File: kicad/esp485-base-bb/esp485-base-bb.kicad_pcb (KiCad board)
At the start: 2 copper layers, 25.4 x 59.7 mm, 20 parts, among them J1 Conn_01x03, J10 Conn_01x04, J11 Conn_01x04, J12 Conn_01x08, J2 Conn_01x03, J3 Conn_01x08, J4 Conn_01x08, J5 Conn_01x04, J6 Conn_01x03, J7 Conn_01x03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

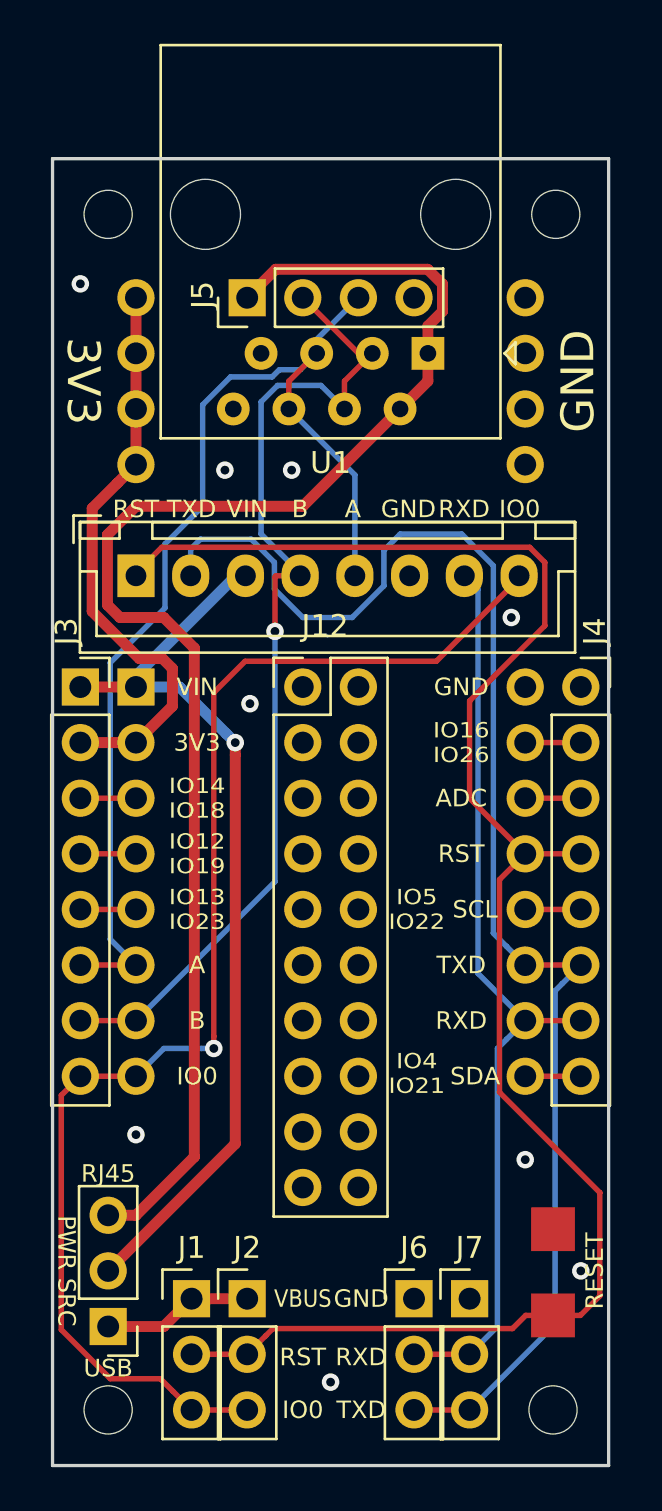
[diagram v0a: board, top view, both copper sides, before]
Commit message: termination resistor added
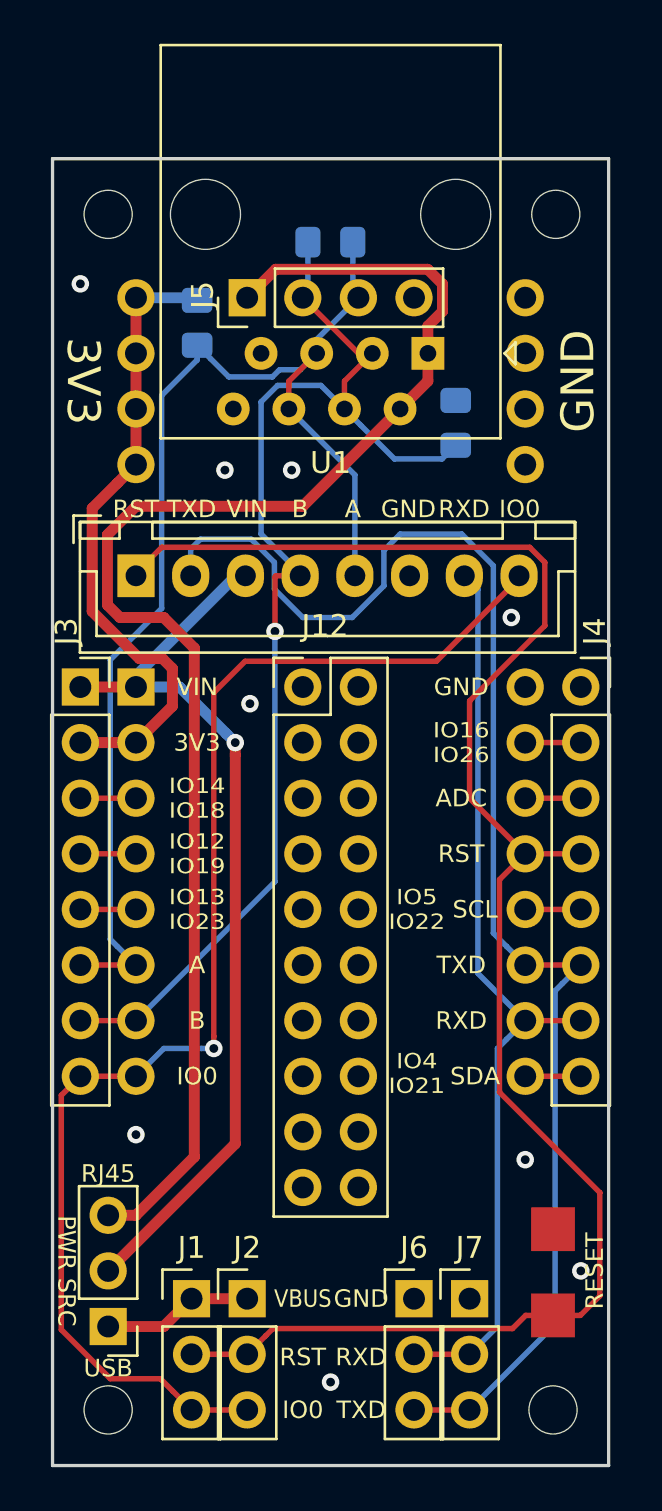
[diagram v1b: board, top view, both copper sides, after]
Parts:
- added R1: 1K, Resistor_SMD:R_0805_2012Metric_Pad1.15x1.40mm_HandSolder, B.Cu at (133.6, 82.4)
- added R2: 120, Resistor_SMD:R_0805_2012Metric_Pad1.15x1.40mm_HandSolder, B.Cu at (139.7, 78.7)
- added R3: 1K, Resistor_SMD:R_0805_2012Metric_Pad1.15x1.40mm_HandSolder, B.Cu at (145.4, 87.0)
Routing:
- net /B: track 47.2 -> 56.1 mm
- net /A: track 51.8 -> 57.7 mm
- net +3V3: track 26.5 -> 29.4 mm
